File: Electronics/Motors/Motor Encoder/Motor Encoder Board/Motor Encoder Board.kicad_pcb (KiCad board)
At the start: 2 copper layers, 30 x 20 mm, 10 parts, among them IC1 AS5600L-ASOM, J1 Conn_01x05_Pin

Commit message: PCB Schematic progress
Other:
- board text added: "ADDR = 0x36"
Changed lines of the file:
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@@
+    (effects (font (size 1 1) (thickness 0.15)) (justify left bottom))
+  )
+  (gr_text "ADDR = 0x36" (at 111.755 54.043) (layer "F.SilkS" knockout)
     (effects (font (size 1 1) (thickness 0.15)) (justify left bottom))
   )

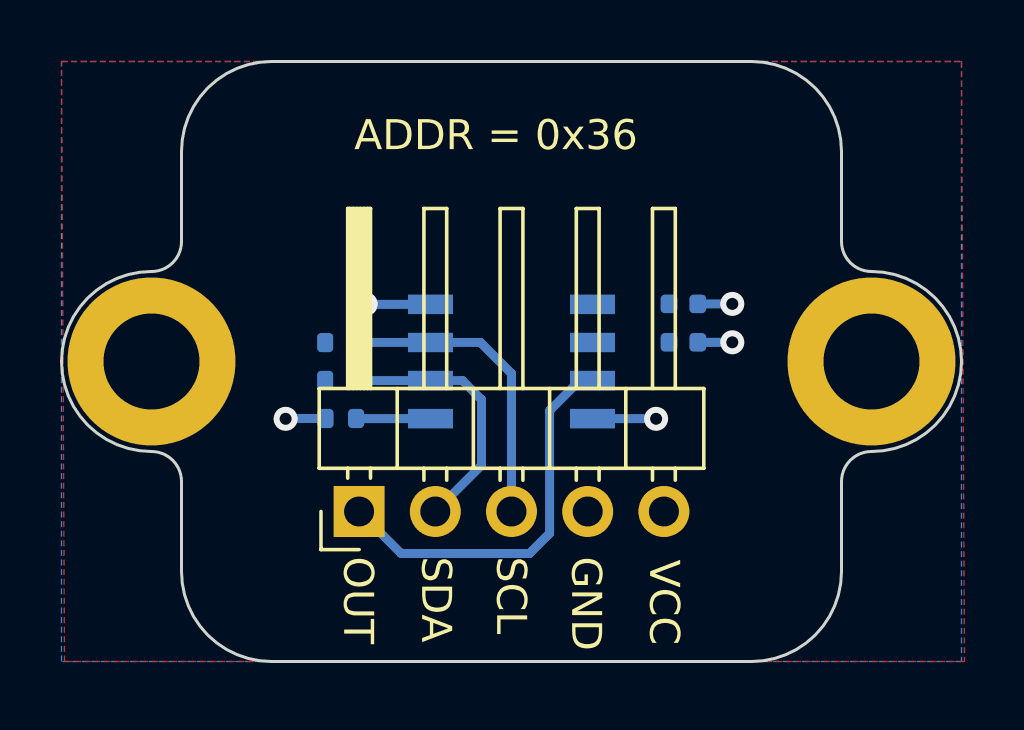
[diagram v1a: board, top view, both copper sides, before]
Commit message: PCB layout progress, spice simulations for power board
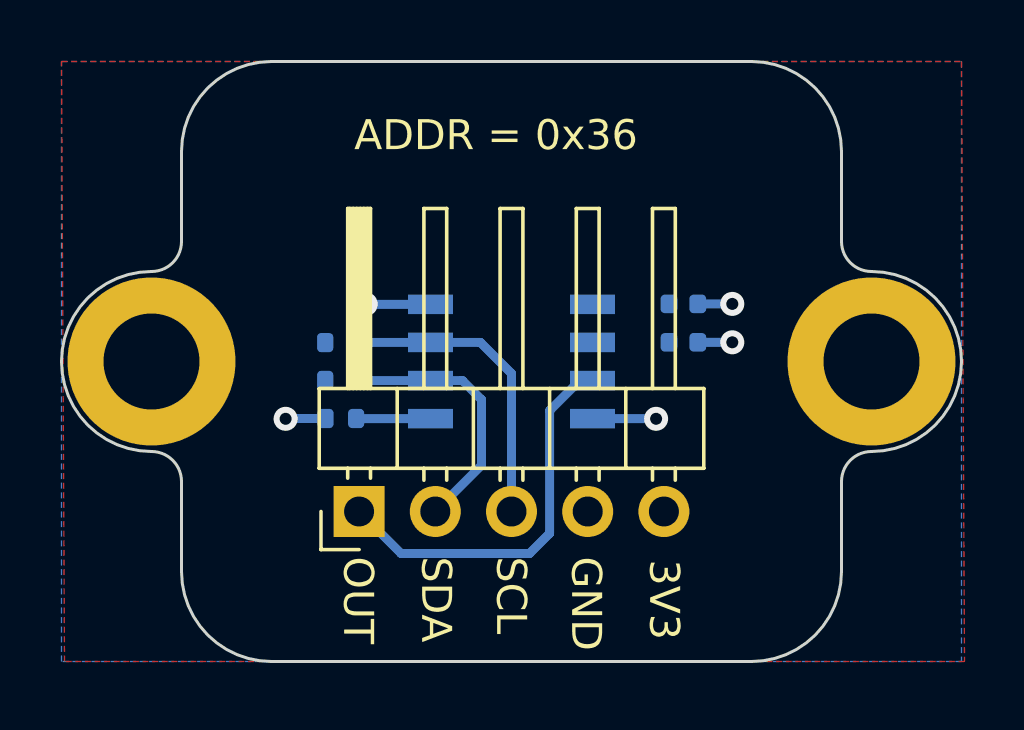
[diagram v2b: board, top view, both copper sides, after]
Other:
- board text added: "3V3"
- board text removed: "VCC"
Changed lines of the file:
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@@
     (effects (font (size 1 1) (thickness 0.15)) (justify left bottom))
   )
-  (gr_text "VCC" (at 121.5 67.6 270) (layer "F.SilkS")
+  (gr_text "3V3" (at 121.5 67.6 270) (layer "F.SilkS")
     (effects (font (size 1 1) (thickness 0.15)) (justify left bottom))
   )
@@
   (segment (start 111.825 62.905) (end 111.82 62.9) (width 0.3) (layer "B.Cu") (net 6))
   (segment (start 114.3 62.905) (end 111.825 62.905) (width 0.3) (layer "B.Cu") (net 6))
-  (zone (net 2) (net_name "GND") (layer "F.Cu") (hatch edge 0.5)
+  (zone locked (net 2) (net_name "GND") (layer "F.Cu") (hatch edge 0.5)
     (connect_pads (clearance 0.5))
     (min_thickness 0.25) (filled_areas_thickness no)
@@
     )
   )
-  (zone (net 1) (net_name "+3V3") (layer "B.Cu") (hatch edge 0.5)
+  (zone locked (net 1) (net_name "+3V3") (layer "B.Cu") (hatch edge 0.5)
     (priority 1)
     (connect_pads (clearance 0.5))

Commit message: Sensor hub board done
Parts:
- G***: moved to F.Cu
- J1: value Conn_01x05_Pin -> JST_2.5mm_1x5; footprint Connector_PinHeader_2.54mm:PinHeader_1x05_P2.54mm_Horizontal -> Connector_JST:JST_XH_B5B-XH-A_1x05_P2.50mm_Vertical
- moved G*** 13.0 mm to (123.5, 55.5), turned to 0 degrees
- moved J1 0.08 mm to (112.0, 66.0), turned to 0 degrees
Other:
- board text added: "_{IMPERIAL MSL} Motor Encoder v1.0"
- board text removed: "MSL Motor Encoder"

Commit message: All boards done
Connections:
- H1 pad 1: GND -> unconnected-(H1-Pad1)
- H2 pad 1: GND -> unconnected-(H2-Pad1)
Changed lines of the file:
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@@
   (setup
     (stackup
-      (layer "F.SilkS" (type "Top Silk Screen"))
+      (layer "F.SilkS" (type "Top Silk Screen") (color "White"))
       (layer "F.Paste" (type "Top Solder Paste"))
-      (layer "F.Mask" (type "Top Solder Mask") (thickness 0.01))
+      (layer "F.Mask" (type "Top Solder Mask") (color "#252525CC") (thickness 0.01))
       (layer "F.Cu" (type "copper") (thickness 0.035))
       (layer "dielectric 1" (type "core") (thickness 1.51) (material "FR4") (epsilon_r 4.5) (loss_tangent 0.02))
       (layer "B.Cu" (type "copper") (thickness 0.035))
-      (layer "B.Mask" (type "Bottom Solder Mask") (thickness 0.01))
+      (layer "B.Mask" (type "Bottom Solder Mask") (color "#252525CC") (thickness 0.01))
       (layer "B.Paste" (type "Bottom Solder Paste"))
-      (layer "B.SilkS" (type "Bottom Silk Screen"))
+      (layer "B.SilkS" (type "Bottom Silk Screen") (color "White"))
       (copper_finish "None")
       (dielectric_constraints no)
@@
       (plotinvisibletext false)
       (sketchpadsonfab false)
-      (subtractmaskfromsilk false)
+      (subtractmaskfromsilk true)
       (outputformat 1)
       (mirror false)
@@
   (net 5 "/SCL")
   (net 6 "/PGO")
+  (net 7 "unconnected-(H1-Pad1)")
+  (net 8 "unconnected-(H2-Pad1)")
   (footprint "MountingHole:MountingHole_3.2mm_M3_DIN965_Pad" (layer "F.Cu")
     (at 129 61)
@@
       (stroke (width 0.05) (type solid)) (fill none) (layer "F.CrtYd"))
     (pad "1" thru_hole circle (at 0 0) (size 5.6 5.6) (drill 3.2) (layers "*.Cu" "*.Mask")
-      (net 2 "GND") (pinfunction "1") (pintype "input"))
+      (net 8 "unconnected-(H2-Pad1)") (pinfunction "1") (pintype "input+no_connect"))
   )
   (footprint "MountingHole:MountingHole_3.2mm_M3_DIN965_Pad" (layer "F.Cu")
@@
       (stroke (width 0.05) (type solid)) (fill none) (layer "F.CrtYd"))
     (pad "1" thru_hole circle (at 0 0) (size 5.6 5.6) (drill 3.2) (layers "*.Cu" "*.Mask")
-      (net 2 "GND") (pinfunction "1") (pintype "input"))
+      (net 7 "unconnected-(H1-Pad1)") (pinfunction "1") (pintype "input+no_connect"))
   )
   (footprint "Connector_JST:JST_XH_B5B-XH-A_1x05_P2.50mm_Vertical" (layer "F.Cu")
@@
     (fp_line (start 12.45 3.4) (end 12.45 -2.35)
       (stroke (width 0.1) (type solid)) (layer "F.Fab"))
-    (pad "1" thru_hole roundrect (at 0 0) (size 1.7 1.95) (drill 0.95) (layers "*.Cu" "*.Mask") (roundrect_rratio 0.147059)
+    (pad "1" thru_hole roundrect (at 0 0) (size 1.7 1.95) (drill 0.95) (layers "*.Cu" "*.Mask") (roundrect_rratio 0.1470588235)
       (net 3 "OUT") (pinfunction "Pin_1") (pintype "passive"))
     (pad "2" thru_hole oval (at 2.5 0) (size 1.7 1.95) (drill 0.95) (layers "*.Cu" "*.Mask")
@@
   (gr_text "_{IMPERIAL MSL}\nMotor Encoder v1.0" (at 124.78 56.37) (layer "B.SilkS" knockout)
     (effects (font (face "Arial") (size 1.2 1.2) (thickness 0.3) bold) (justify left bottom mirror))
-    (render_cache "_{IMPERIAL MSL}\nMotor Encoder v1.0" -0
+    (render_cache "_{IMPERIAL MSL}\nMotor Encoder v1.0" 0
       (polygon
         (pts
